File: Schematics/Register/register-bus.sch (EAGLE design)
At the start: 17 parts

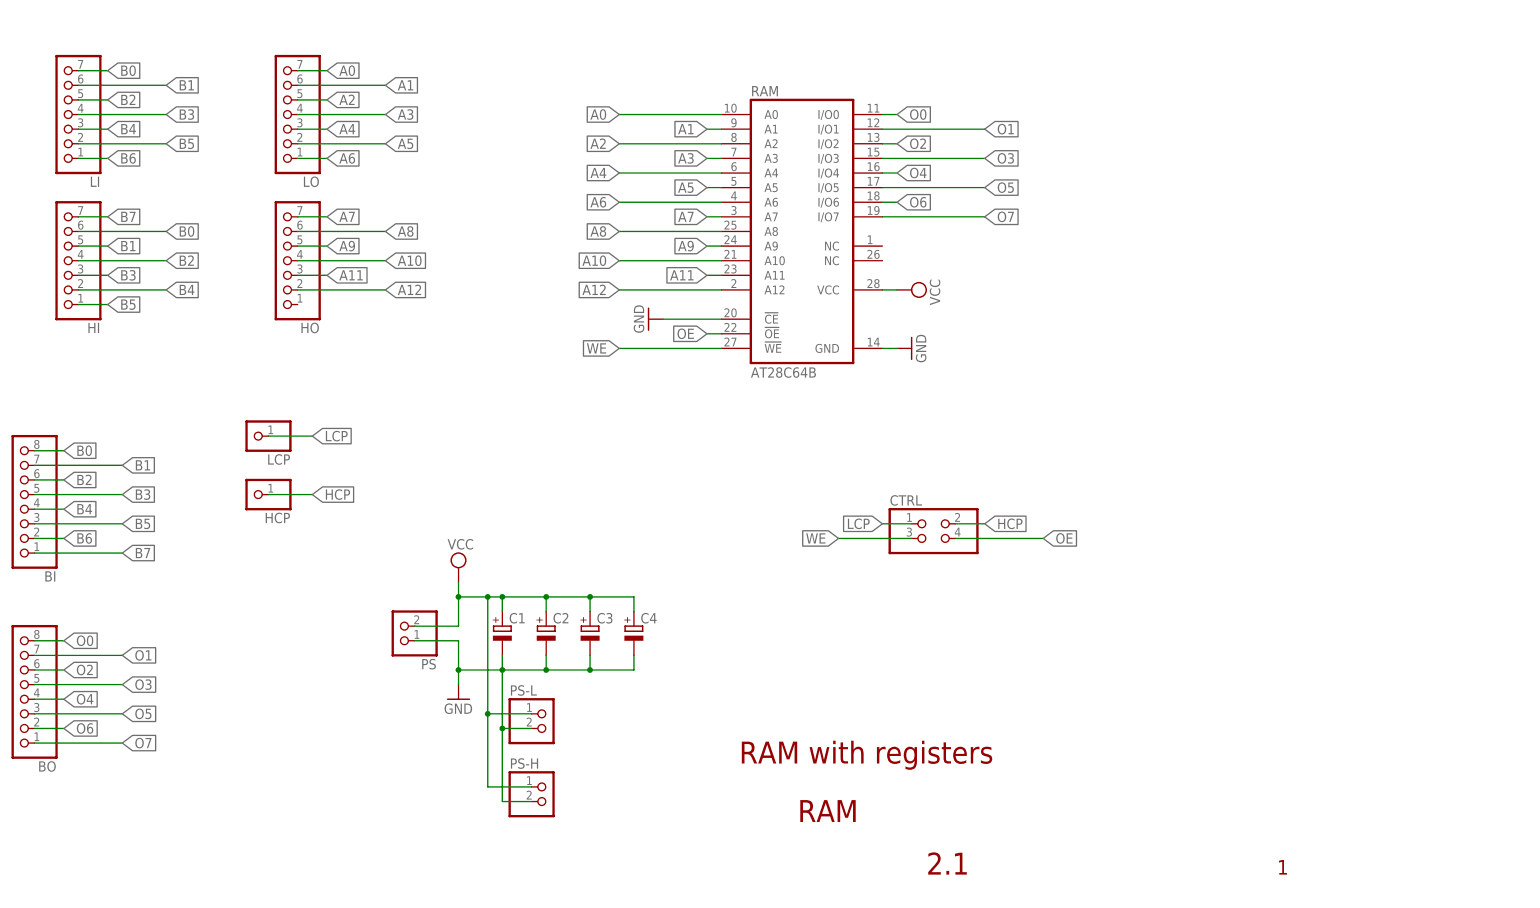
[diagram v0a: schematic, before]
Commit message: Register and RAM modules.
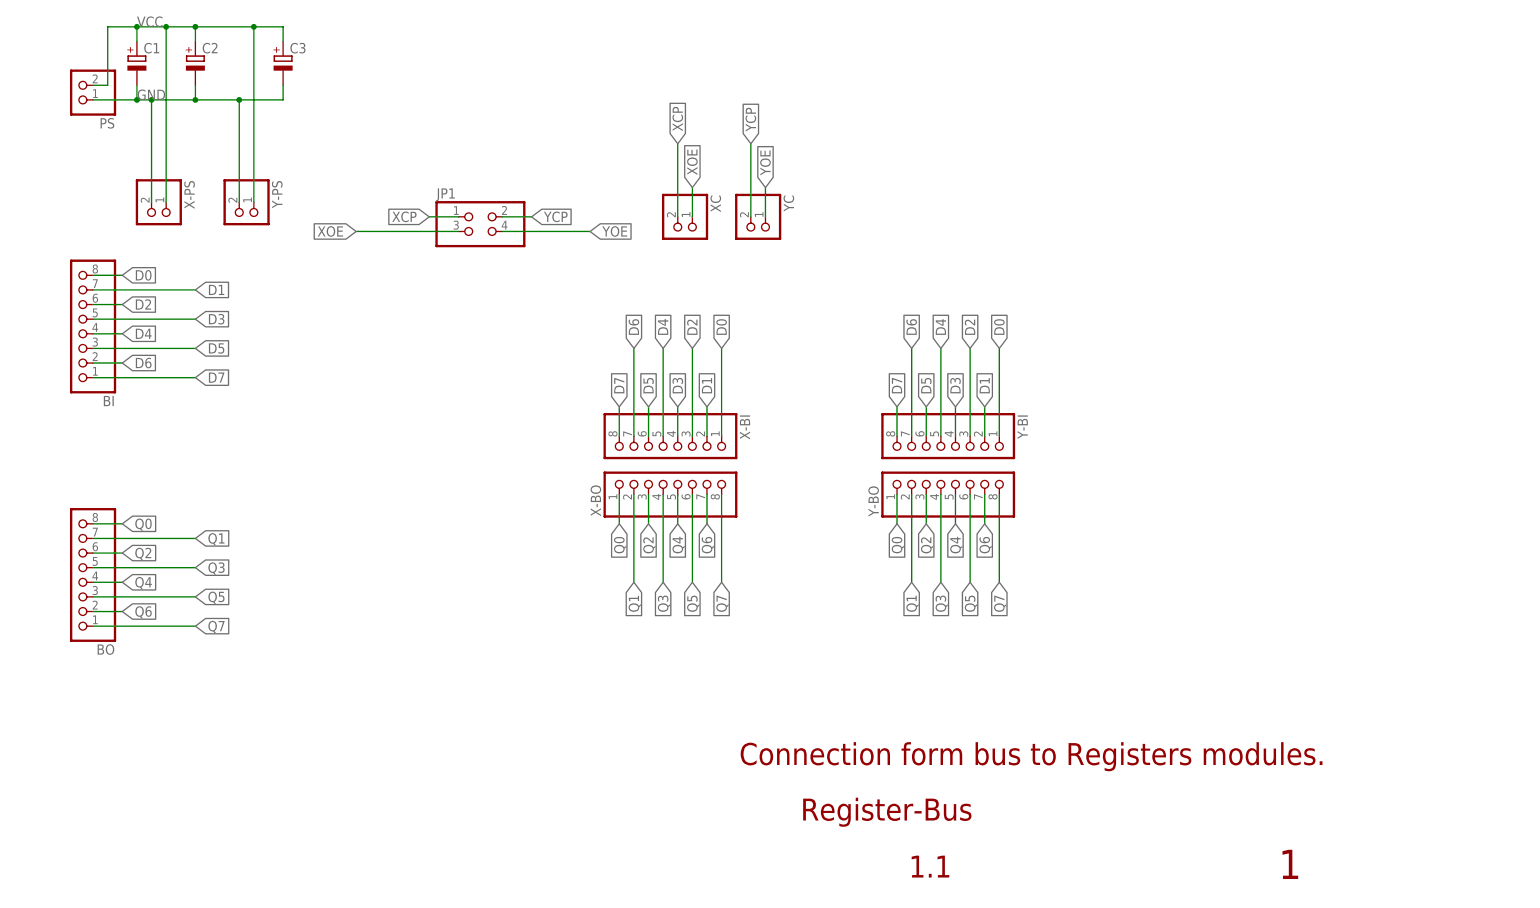
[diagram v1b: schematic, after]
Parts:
- removed C4: (no value), rcl:CPOL-EUE2.5-6
- removed CTRL: (no value), pinhead:PINHD-2X2
- removed HCP, LCP: (no value), pinhead:PINHD-1X1
- removed HI, HO, LI, LO: (no value), pinhead:PINHD-1X7
- removed PS-H, PS-L: (no value), pinhead:PINHD-1X2
- removed RAM: AT28C64B, memory-nec:28C64C
- added JP1: (no value), pinhead:PINHD-2X2
- added X-BI, X-BO, Y-BI, Y-BO: (no value), pinhead:PINHD-1X8
- added X-PS, XC, Y-PS, YC: (no value), pinhead:PINHD-1X2
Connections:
- removed net A0: LO.7, RAM.A0
- removed net A1: LO.6, RAM.A1
- removed net A10: HO.4, RAM.A10
- removed net A11: HO.3, RAM.A11
- removed net A12: HO.2, RAM.A12
- removed net A2: LO.5, RAM.A2
- removed net A3: LO.4, RAM.A3
- removed net A4: LO.3, RAM.A4
- removed net A5: LO.2, RAM.A5
- removed net A6: LO.1, RAM.A6
- removed net A7: HO.7, RAM.A7
- removed net A8: HO.6, RAM.A8
- removed net A9: HO.5, RAM.A9
- removed net B0: BI.8, HI.6, LI.7
- removed net B1: BI.7, HI.5, LI.6
- removed net B2: BI.6, HI.4, LI.5
- removed net B3: BI.5, HI.3, LI.4
- removed net B4: BI.4, HI.2, LI.3
- removed net B5: BI.3, HI.1, LI.2
- removed net B6: BI.2, LI.1
- removed net B7: BI.1, HI.7
- removed net HCP: CTRL.2, HCP.1
- removed net LCP: CTRL.1, LCP.1
- removed net O0: BO.8, RAM.I/O0
- removed net O1: BO.7, RAM.I/O1
- removed net O2: BO.6, RAM.I/O2
- removed net O3: BO.5, RAM.I/O3
- removed net O4: BO.4, RAM.I/O4
- removed net O5: BO.3, RAM.I/O5
- removed net O6: BO.2, RAM.I/O6
- removed net O7: BO.1, RAM.I/O7
- removed net OE: CTRL.4, RAM.!OE
- removed net WE: CTRL.3, RAM.!WE
- new net D0: BI.8, X-BI.1, Y-BI.1
- new net D1: BI.7, X-BI.2, Y-BI.2
- new net D2: BI.6, X-BI.3, Y-BI.3
- new net D3: BI.5, X-BI.4, Y-BI.4
- new net D4: BI.4, X-BI.5, Y-BI.5
- new net D5: BI.3, X-BI.6, Y-BI.6
- new net D6: BI.2, X-BI.7, Y-BI.7
- new net D7: BI.1, X-BI.8, Y-BI.8
- new net Q0: BO.8, X-BO.1, Y-BO.1
- new net Q1: BO.7, X-BO.2, Y-BO.2
- new net Q2: BO.6, X-BO.3, Y-BO.3
- new net Q3: BO.5, X-BO.4, Y-BO.4
- new net Q4: BO.4, X-BO.5, Y-BO.5
- new net Q5: BO.3, X-BO.6, Y-BO.6
- new net Q6: BO.2, X-BO.7, Y-BO.7
- new net Q7: BO.1, X-BO.8, Y-BO.8
- new net XCP: JP1.1, XC.2
- new net XOE: JP1.3, XC.1
- new net YCP: JP1.2, YC.2
- new net YOE: JP1.4, YC.1
- net GND: now also X-PS.2, Y-PS.2; no longer C4.-, PS-H.2, PS-L.2, RAM.!CE, RAM.GND
- net VCC: now also X-PS.1, Y-PS.1; no longer C4.+, PS-H.1, PS-L.1, RAM.VCC
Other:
- note added: "1.1"
- note added: "Connection form bus to Registers modules."
- note added: "Register-Bus"
- note removed: "2.1"
- note removed: "RAM"
- note removed: "RAM with registers"
- moved on the sheet: BI, BO, C1, C2, C3, PS
